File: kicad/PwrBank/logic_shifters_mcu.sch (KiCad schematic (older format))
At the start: 3 parts

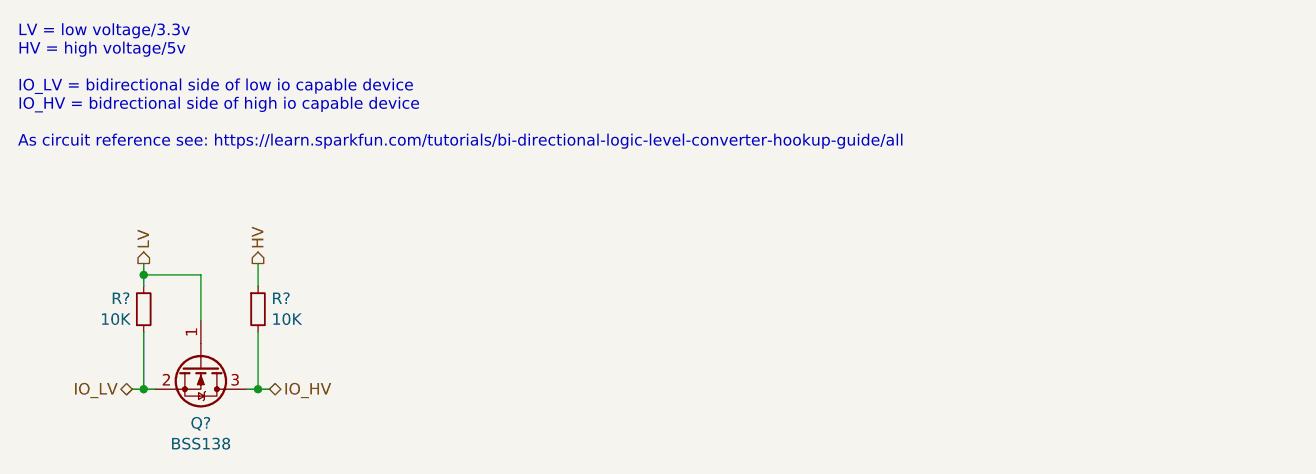
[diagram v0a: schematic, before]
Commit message: Working on/off system with safe shutdown and deepsleep inbetween
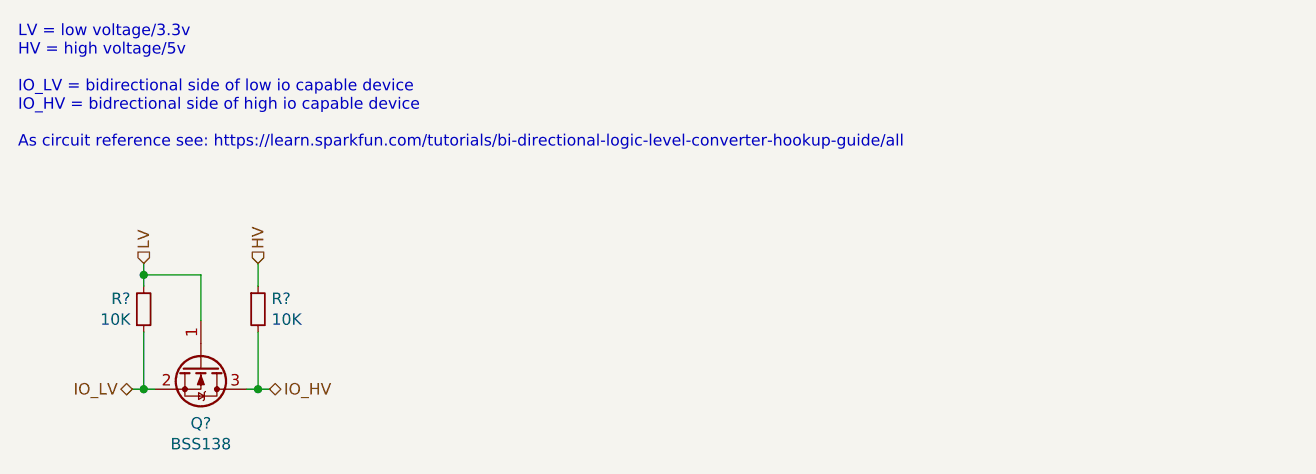
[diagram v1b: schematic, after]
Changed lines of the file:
@@
 $Descr A4 11693 8268
 encoding utf-8
-Sheet 8 8
+Sheet 8 9
 Title "Logic Shifters MCU"
 Date "2021-07-17"
@@
 Comment4 ""
 $EndDescr
-Text HLabel 3750 2300 1    50   Output ~ 0
+Text HLabel 3750 2300 1    50   Input ~ 0
 HV
-Text HLabel 3250 2300 1    50   Output ~ 0
+Text HLabel 3250 2300 1    50   Input ~ 0
 LV
 $Comp
@@
 U 1 1 60F399FD
 P 3250 2500
+AR Path="/60F2D9E7/60F3980E/60F399FD" Ref="R?"  Part="1"
+AR Path="/60F2D9E7/60F56C27/60F399FD" Ref="R?"  Part="1"
 F 0 "R?" H 3192 2454 50  0000 R CNN
 F 1 "10K" H 3192 2545 50  0000 R CNN
@@
 U 1 1 60F39B1A
 P 3750 2500
+AR Path="/60F2D9E7/60F3980E/60F39B1A" Ref="R?"  Part="1"
+AR Path="/60F2D9E7/60F56C27/60F39B1A" Ref="R?"  Part="1"
 F 0 "R?" H 3809 2546 50  0000 L CNN
 F 1 "10K" H 3809 2455 50  0000 L CNN
@@
 U 1 1 60F3AB7E
 P 3500 2750
+AR Path="/60F2D9E7/60F3980E/60F3AB7E" Ref="Q?"  Part="1"
+AR Path="/60F2D9E7/60F56C27/60F3AB7E" Ref="Q?"  Part="1"
 F 0 "Q?" V 3749 2750 50  0000 C CNN
 F 1 "BSS138" V 3840 2750 50  0000 C CNN

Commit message: UPDATE KICAD SOURCEFILES
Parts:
- R18, R19: renamed from R?; footprint (none) -> Resistor_SMD:R_0805_2012Metric_Pad1.20x1.40mm_HandSolder
- gave numbers to parts that had none: 1
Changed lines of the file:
@@
 $Descr A4 11693 8268
 encoding utf-8
-Sheet 8 9
+Sheet 7 8
 Title "Logic Shifters MCU"
 Date "2021-07-17"
@@
 LV
 $Comp
-L Device:R_Small R?
+L Device:R_Small R18
 U 1 1 60F399FD
 P 3250 2500
-AR Path="/60F2D9E7/60F3980E/60F399FD" Ref="R?"  Part="1"
-AR Path="/60F2D9E7/60F56C27/60F399FD" Ref="R?"  Part="1"
-F 0 "R?" H 3192 2454 50  0000 R CNN
+AR Path="/60F2D9E7/60F3980E/60F399FD" Ref="R18"  Part="1"
+AR Path="/60F2D9E7/60F56C27/60F399FD" Ref="R16"  Part="1"
+F 0 "R18" H 3192 2454 50  0000 R CNN
 F 1 "10K" H 3192 2545 50  0000 R CNN
-F 2 "" H 3250 2500 50  0001 C CNN
+F 2 "Resistor_SMD:R_0805_2012Metric_Pad1.20x1.40mm_HandSolder" H 3250 2500 50  0001 C CNN
 F 3 "~" H 3250 2500 50  0001 C CNN
 	1    3250 2500
@@
 $EndComp
 $Comp
-L Device:R_Small R?
+L Device:R_Small R19
 U 1 1 60F39B1A
 P 3750 2500
-AR Path="/60F2D9E7/60F3980E/60F39B1A" Ref="R?"  Part="1"
-AR Path="/60F2D9E7/60F56C27/60F39B1A" Ref="R?"  Part="1"
-F 0 "R?" H 3809 2546 50  0000 L CNN
+AR Path="/60F2D9E7/60F3980E/60F39B1A" Ref="R19"  Part="1"
+AR Path="/60F2D9E7/60F56C27/60F39B1A" Ref="R17"  Part="1"
+F 0 "R19" H 3809 2546 50  0000 L CNN
 F 1 "10K" H 3809 2455 50  0000 L CNN
-F 2 "" H 3750 2500 50  0001 C CNN
+F 2 "Resistor_SMD:R_0805_2012Metric_Pad1.20x1.40mm_HandSolder" H 3750 2500 50  0001 C CNN
 F 3 "~" H 3750 2500 50  0001 C CNN
 	1    3750 2500
@@
 LV = low voltage/3.3v\nHV = high voltage/5v\n\nIO_LV = bidirectional side of low io capable device\nIO_HV = bidrectional side of high io capable device\n\nAs circuit reference see: https://learn.sparkfun.com/tutorials/bi-directional-logic-level-converter-hookup-guide/all
 $Comp
-L Transistor_FET:BSS138 Q?
+L Transistor_FET:BSS138 Q4
 U 1 1 60F3AB7E
 P 3500 2750
-AR Path="/60F2D9E7/60F3980E/60F3AB7E" Ref="Q?"  Part="1"
-AR Path="/60F2D9E7/60F56C27/60F3AB7E" Ref="Q?"  Part="1"
-F 0 "Q?" V 3749 2750 50  0000 C CNN
+AR Path="/60F2D9E7/60F3980E/60F3AB7E" Ref="Q4"  Part="1"
+AR Path="/60F2D9E7/60F56C27/60F3AB7E" Ref="Q3"  Part="1"
+F 0 "Q4" V 3749 2750 50  0000 C CNN
 F 1 "BSS138" V 3840 2750 50  0000 C CNN
 F 2 "Package_TO_SOT_SMD:SOT-23" H 3700 2675 50  0001 L CIN
